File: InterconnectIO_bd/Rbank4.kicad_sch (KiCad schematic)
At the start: 48 parts, among them K10 TQ2-5, K11 TQ2-5, K12 TQ2-5, K13 TQ2-5, K14 TQ2-5, K15 TQ2-5, K16 TQ2-5, K17 TQ2-5, K18 TQ2-5

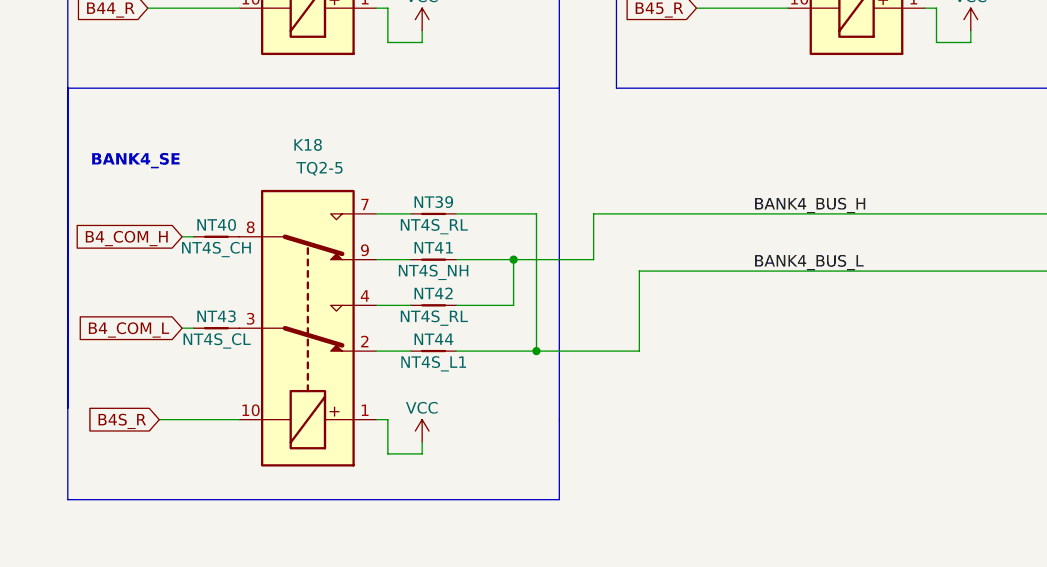
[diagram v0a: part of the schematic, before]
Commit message: Reverse COM_H and COM_L on relay Bank
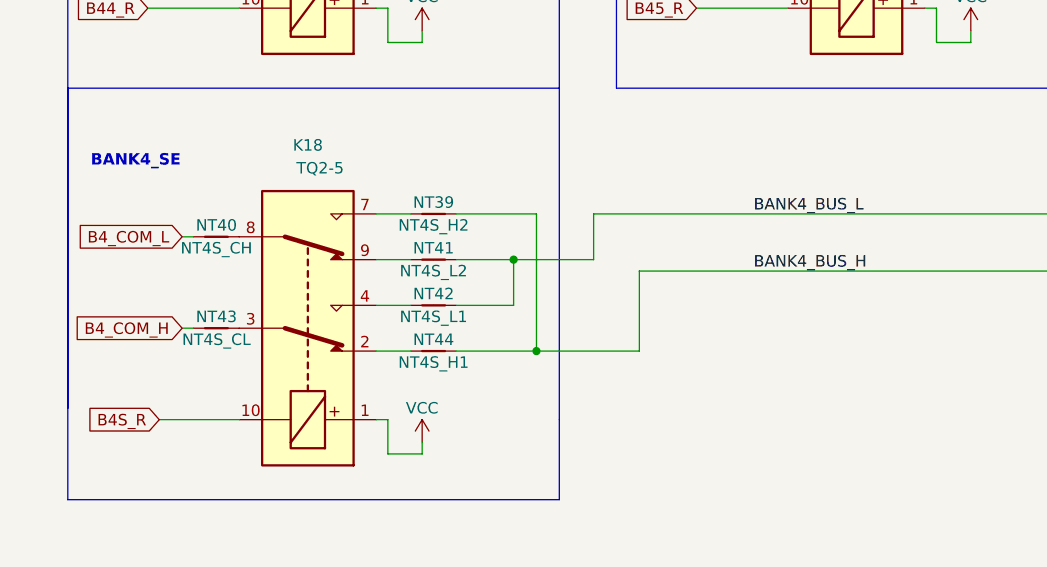
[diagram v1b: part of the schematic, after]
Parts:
- NT39: value NT4S_RL -> NT4S_H2
- NT41: value NT4S_NH -> NT4S_L2
- NT42: value NT4S_RL -> NT4S_L1
- NT44: value NT4S_L1 -> NT4S_H1
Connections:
- net B4_COM_H: now also NT43.1; no longer NT40.1
- net B4_COM_L: now also NT40.1; no longer NT43.1
- net BANK4_BUS_H: now also NT23.1, NT24.1, NT25.1, NT26.1, NT31.1, NT32.1, NT33.1, NT34.1, NT39.2, NT44.2; no longer NT27.1, NT28.1, NT29.1, NT30.1, NT35.1, NT36.1, NT37.1, NT38.1, NT41.2, NT42.2
- net BANK4_BUS_L: now also NT27.1, NT28.1, NT29.1, NT30.1, NT35.1, NT36.1, NT37.1, NT38.1, NT41.2, NT42.2; no longer NT23.1, NT24.1, NT25.1, NT26.1, NT31.1, NT32.1, NT33.1, NT34.1, NT39.2, NT44.2
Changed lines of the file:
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@@
     (effects (font (size 1.27 1.27) (thickness 0.254) bold) (justify left bottom))
   )
-  (label "BANK4_BUS_H" (at 97.79 123.19 0) (fields_autoplaced)
+  (label "BANK4_BUS_L" (at 97.79 123.19 0) (fields_autoplaced)
     (effects (font (size 1.27 1.27)) (justify left bottom))
   )
@@
     (effects (font (size 1.27 1.27)) (justify left bottom))
   )
-  (label "BANK4_BUS_L" (at 97.79 129.54 0) (fields_autoplaced)
+  (label "BANK4_BUS_H" (at 97.79 129.54 0) (fields_autoplaced)
     (effects (font (size 1.27 1.27)) (justify left bottom))
   )
@@
     )
   )
-  (global_label "B4_COM_H" (shape input) (at 34.29 125.73 180) (fields_autoplaced)
+  (global_label "B4_COM_L" (shape input) (at 34.29 125.73 180) (fields_autoplaced)
     (effects (font (size 1.27 1.27)) (justify right))
-    (property "Intersheetrefs" "${INTERSHEET_REFS}" (at 22.0798 125.6506 0)
+    (property "Intersheetrefs" "${INTERSHEET_REFS}" (at 21.8895 125.73 0)
       (effects (font (size 1.27 1.27)) (justify right) hide)
     )
   )
-  (global_label "B4_COM_L" (shape input) (at 34.29 135.89 180) (fields_autoplaced)
+  (global_label "B4_COM_H" (shape input) (at 34.29 135.89 180) (fields_autoplaced)
     (effects (font (size 1.27 1.27)) (justify right))
-    (property "Intersheetrefs" "${INTERSHEET_REFS}" (at 22.3821 135.8106 0)
+    (property "Intersheetrefs" "${INTERSHEET_REFS}" (at 21.5871 135.89 0)
       (effects (font (size 1.27 1.27)) (justify right) hide)
     )
@@
       (effects (font (size 1.27 1.27)))
     )
-    (property "Value" "NT4S_NH" (at 62.23 129.54 0)
+    (property "Value" "NT4S_L2" (at 62.23 129.54 0)
       (effects (font (size 1.27 1.27)))
     )
@@
       (effects (font (size 1.27 1.27)))
     )
-    (property "Value" "NT4S_RL" (at 62.23 124.46 0)
+    (property "Value" "NT4S_H2" (at 62.23 124.46 0)
       (effects (font (size 1.27 1.27)))
     )
@@
       (effects (font (size 1.27 1.27)))
     )
-    (property "Value" "NT4S_RL" (at 62.23 134.62 0)
+    (property "Value" "NT4S_L1" (at 62.23 134.62 0)
       (effects (font (size 1.27 1.27)))
     )
@@
       (effects (font (size 1.27 1.27)))
     )
-    (property "Value" "NT4S_L1" (at 62.23 139.7 0)
-      (effects (font (size 1.27 1.27)))
-    )
+    (property "Value" "NT4S_H1" (at 62.23 139.7 0)
+      (effects (font (size 1.27 1.27)))
+    )
